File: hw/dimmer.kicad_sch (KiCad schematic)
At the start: 40 parts, among them J4 Screw_Terminal_01x02, Q10 MMBT3904, Q11 MMBT3906, Q13 IPN80R900P7, Q14 IPN80R900P7, Q9 MMBT3904, U2 PC817XI, U3 H11L1SR2M, U4 PC817XI

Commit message: Update design
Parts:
- R16: renamed from R14; value 90k -> 91k
- R17: renamed from R15; value 90k -> 91k
- R18, R19: value 90k -> 91k
- renumbered C10 to C11, C9 to C12, C11 to C13, C12 to C14, C13 to C15, C14 to C16, D7 to D10, D10 to D11, D11 to D13, D5 to D6, D6 to D7, J4 to J5, Q9 to Q2, Q10 to Q3, Q11 to Q4, Q13 to Q5, Q14 to Q6, R17 to R20, R16 to R21, R13 to R22, R12 to R23, R22 to R25, R25 to R26, R23 to R27, R20 to R28, R21 to R29, R26 to R30, R27 to R31, U2 to U3, U3 to U4, U4 to U5
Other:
- title: LEDDs -> Dimmer
- moved on the sheet: C11, C12, C13, C14, C15, C16, D10, D11, D12, D13, D6, D7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

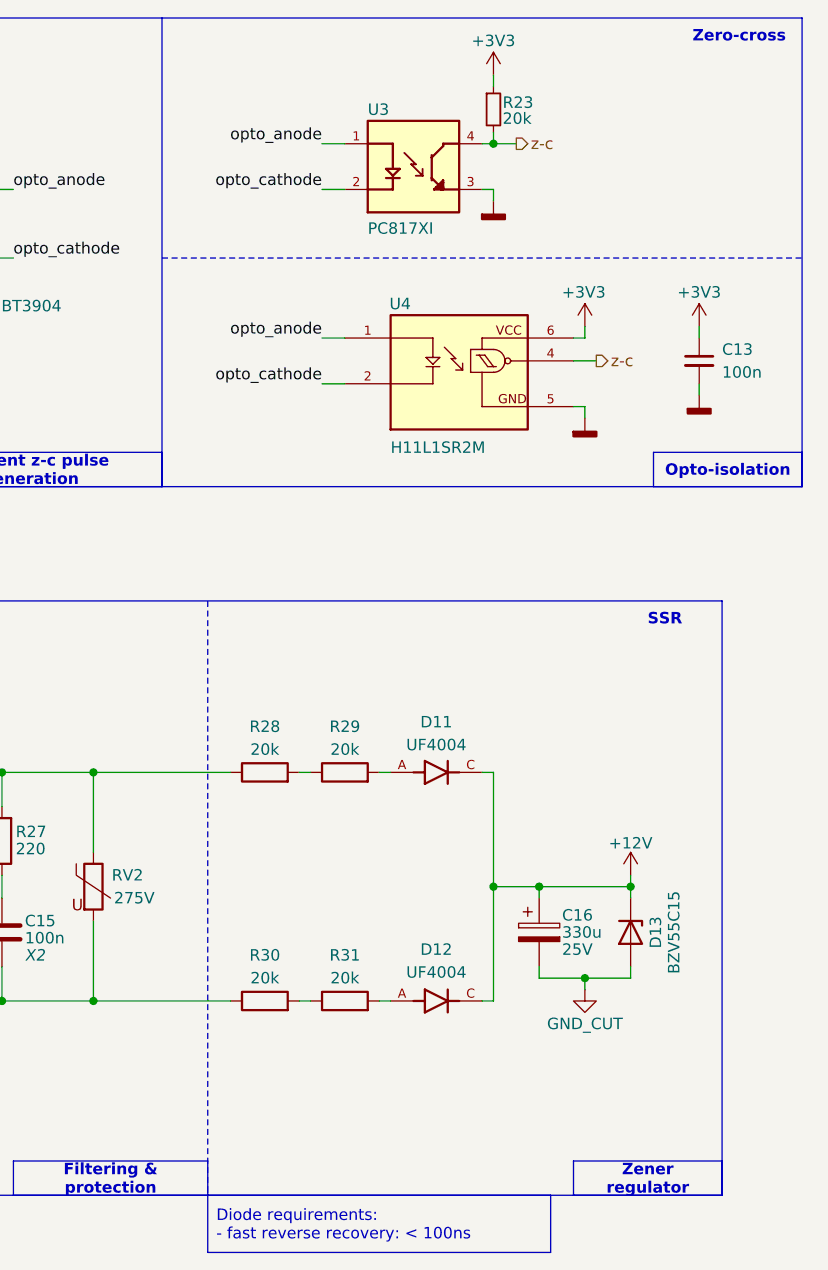
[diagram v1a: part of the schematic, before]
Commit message: Fix included libraries. Arrange schematic notes. Add mechanical parts to schematic.
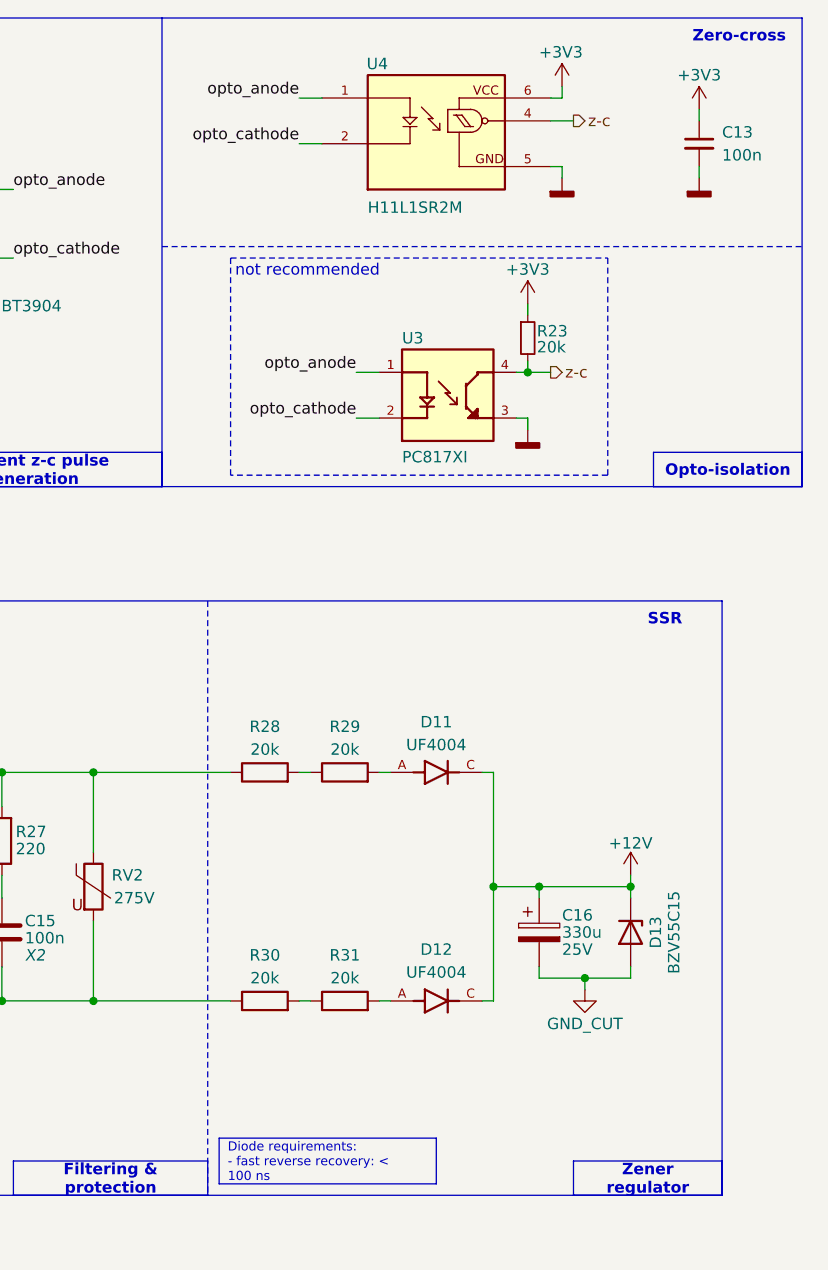
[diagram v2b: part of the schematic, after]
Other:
- note added: "not recommended"
- moved on the sheet: C13, R23, U3, U4
